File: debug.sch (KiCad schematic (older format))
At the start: 46 parts, among them J1 ZX62D-AB-5P8, P1 LPC-Link, P2 UART, P3 JTAG, P4 Cortex-Debug, U1 93C46, U2 PRTR5V0U2X, U3 FT2232H, U4 LD1117S33CTR, X1 12MHz

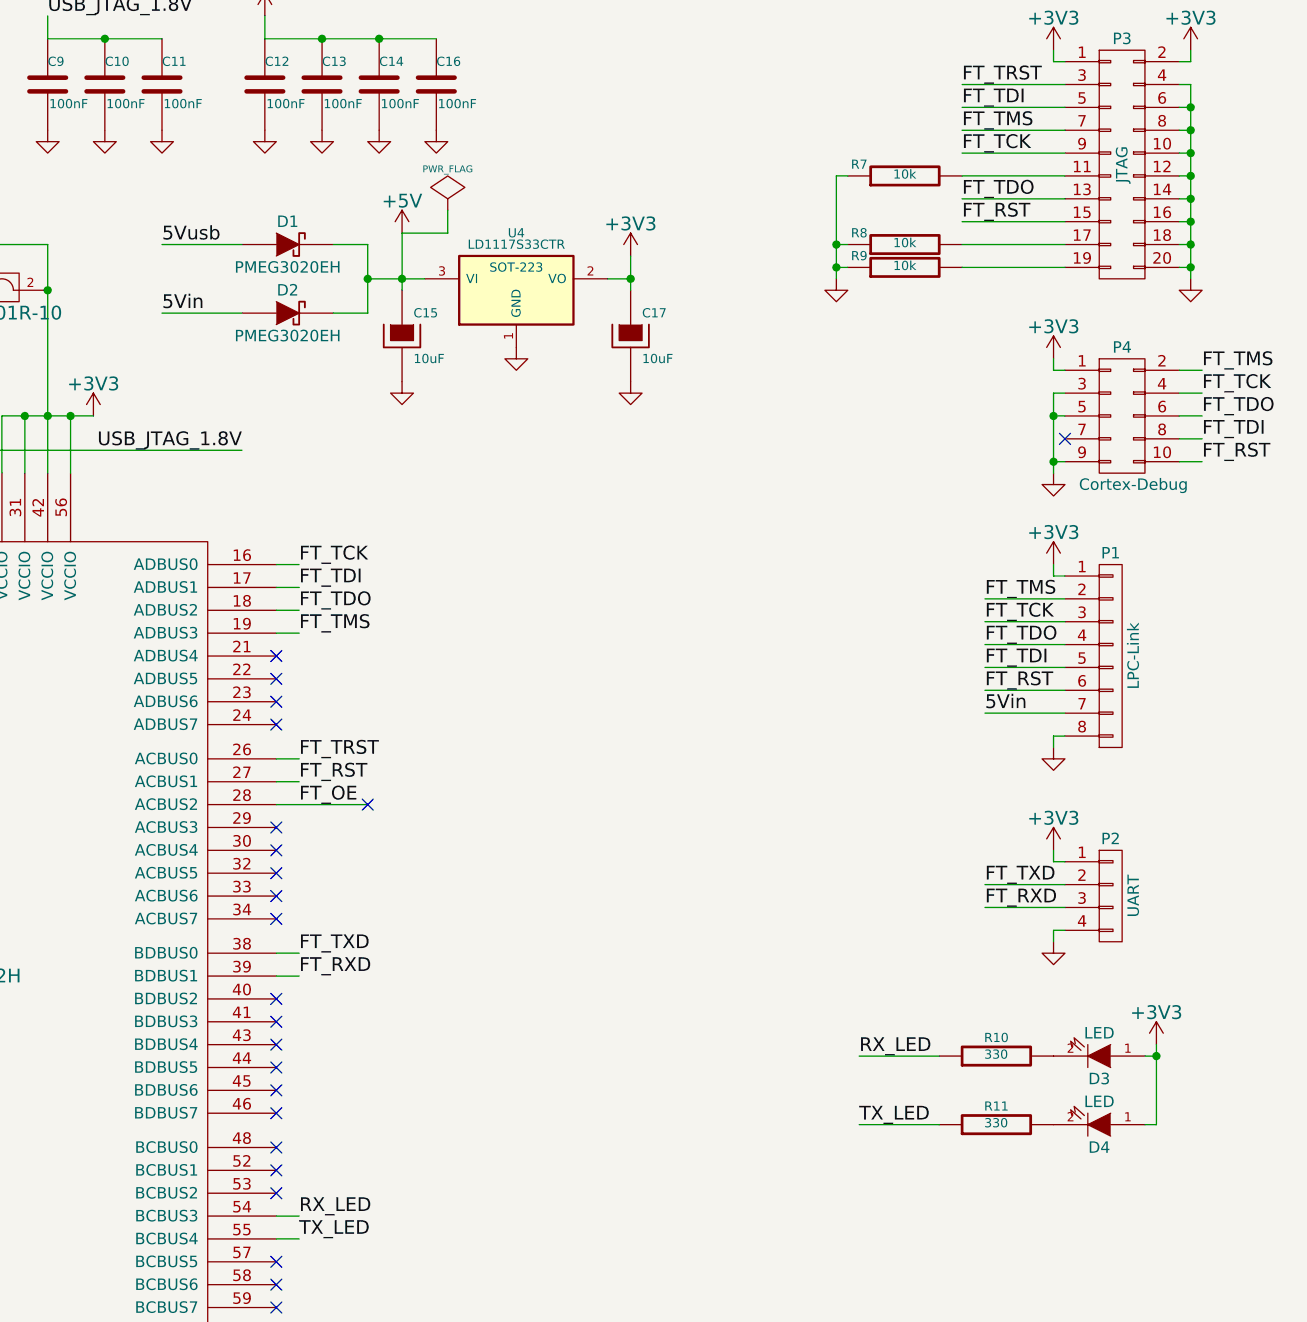
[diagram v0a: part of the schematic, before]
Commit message: sch mejorado, erc ok, netlist generado
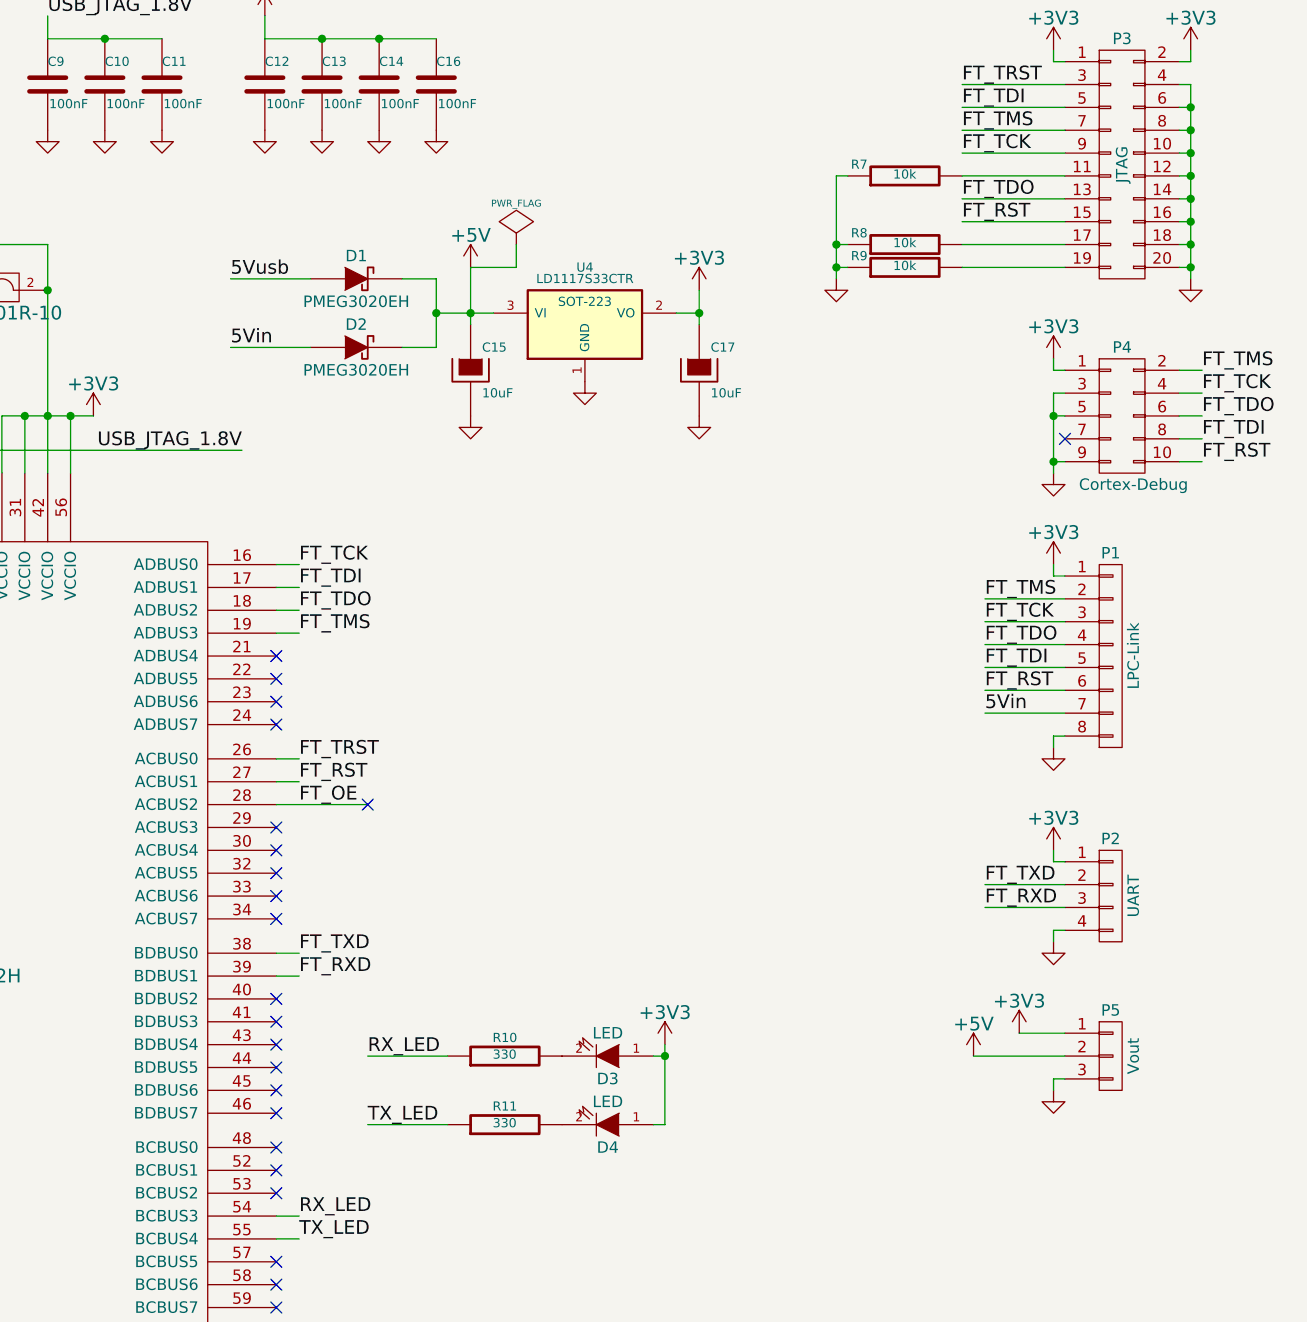
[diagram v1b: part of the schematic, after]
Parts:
- added P5: Vout, symbol CONN_01X03
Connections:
- net +3V3: now also P5.1 (P1)
- net +5V: now also P5.2 (P2)
- net GND: now also P5.3 (P3)
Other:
- moved on the sheet: C15, C17, D1, D2, D3, D4, R10, R11, U4

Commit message: working on footprint association
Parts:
- C1, C10, C11, C12, C13, C14, C16, C2, C3, C4, C5, C7, C9: footprint c_0805 -> Capacitors_SMD:C_0805_HandSoldering
- C15, C17, C6, C8: footprint c_1206_tantalio -> Capacitors_Tantalum_SMD:TantalC_SizeA_EIA-3216_HandSoldering
- D3, D4: footprint (none) -> LEDs:LED-0805
- FB1, FB2, FB3, FB4, R1, R10, R11, R2, R3, R4, R5, R6, R7, R8, R9: footprint SM0805 -> (none)
- J1: footprint USB_microAB_ZX62-AB-5P8 -> (none)
- U1: footprint -SOIC8 -> (none)
- U2: footprint sot143B -> (none); Descripcion (none) -> TVS DIODE 5.5VWM SOT143B; Descripción TVS DIODE 5.5VWM SOT143B -> (none); Footprint SOT-143B -> (none)
- U3: footprint LQFP64-M05 -> (none)
- U4: footprint SOT-223 -> (none)
- X1: footprint 4-SMD,_No_Lead_(DFN,_LCC) -> (none)
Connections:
- net CHJ3: no longer names the net of FB1.1, J1.6 (P6), J1.7 (P7), J1.8 (P8), J1.9 (P9), U2.1 (GND)
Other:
- moved on the sheet: U2

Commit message: footprint assoc done, working on placement
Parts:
- D1, D2: footprint (none) -> Diodes_SMD:SOD-123
- FB1, FB2, FB3, FB4: footprint (none) -> Capacitors_SMD:C_0805_HandSoldering
- J1: footprint (none) -> MicroUSB-ZX62AB:USB_microAB_ZX62-AB&B-5PA-11
- P1: footprint (none) -> Pin_Headers:Pin_Header_Straight_1x08
- P2: footprint (none) -> Pin_Headers:Pin_Header_Straight_1x04
- P3: footprint (none) -> Pin_Headers:Pin_Header_Straight_2x10
- P4: footprint (none) -> riaconnect:Pin_Array_5x2_1.27mm_SMD
- P5: footprint (none) -> Pin_Headers:Pin_Header_Straight_1x03
- R1, R10, R11, R2, R3, R4, R5, R6, R7, R8, R9: footprint (none) -> Resistors_SMD:R_0805_HandSoldering
- U1: footprint (none) -> ref-packages:-SOIC8
- U2: footprint (none) -> opendous:SOT-143B
- U3: footprint (none) -> oaa_smd_qfp:LQFP64-M05
- U4: footprint (none) -> opendous:SOT223_Opendous
- X1: footprint (none) -> MF-SM030:FA238V-XTAL
